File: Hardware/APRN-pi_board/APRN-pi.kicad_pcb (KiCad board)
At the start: 2 copper layers, 65 x 56.5 mm, 21 parts, among them J1 Raspberry_Pi_2_3, J2 Conn_Coaxial, J3 Amplifier Jumper, Q1 2N3906, U1 DRA818V

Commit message: Hook up voltage regulator
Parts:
- added C4: 10u, Capacitor_SMD:C_0805_2012Metric, F.Cu at (161.5, 104.5)
- added C5: 0.1u, Capacitor_SMD:C_0805_2012Metric, F.Cu at (161.0, 98.5)
- added J4: Screw_Terminal_01x02, TerminalBlock:TerminalBlock_bornier-2_P5.08mm, F.Cu at (169.5, 111.6)
- added U2: L7805, Package_TO_SOT_THT:TO-220-3_Vertical, F.Cu at (170.0, 99.5)
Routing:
- net +5V: track 81.2 -> 102.5 mm, vias 0 -> 2
- net Net-(C4-Pad1): track 0.00 -> 15.6 mm

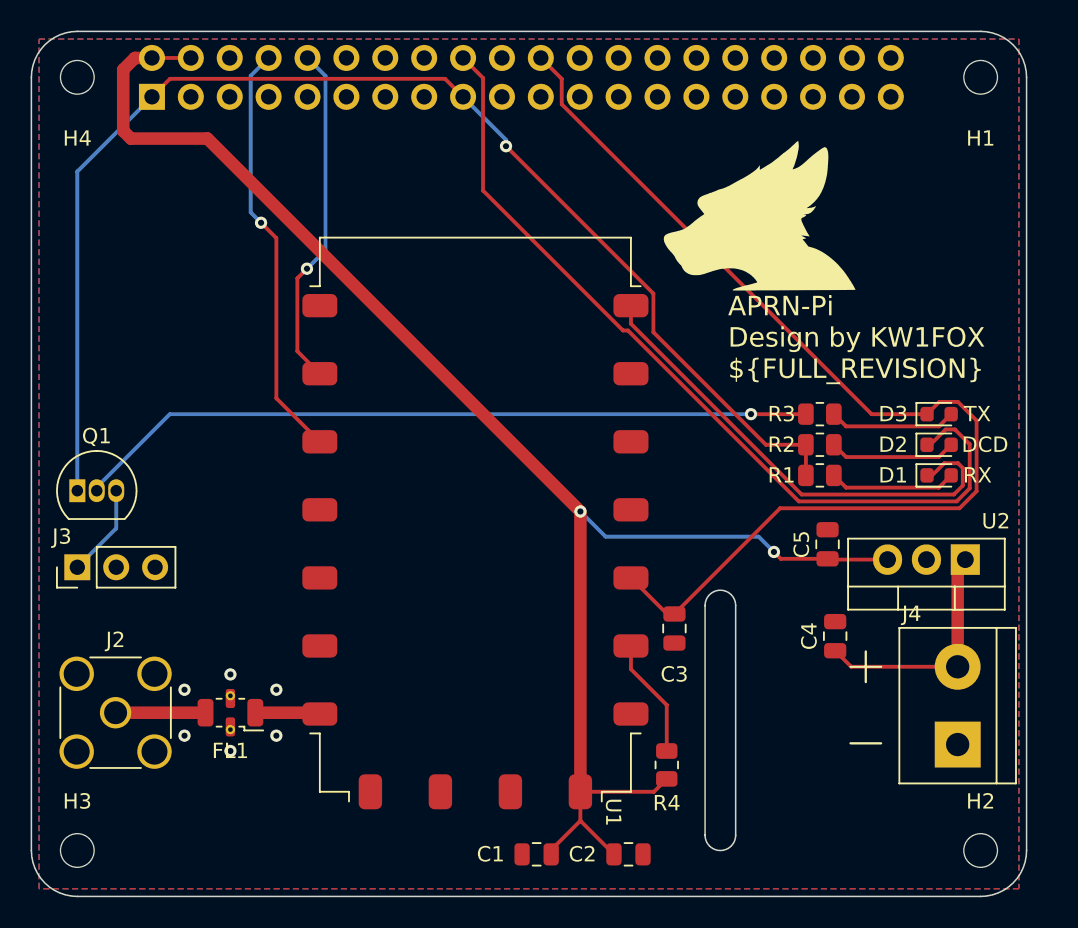
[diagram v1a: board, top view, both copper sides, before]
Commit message: More power and audio cleanup
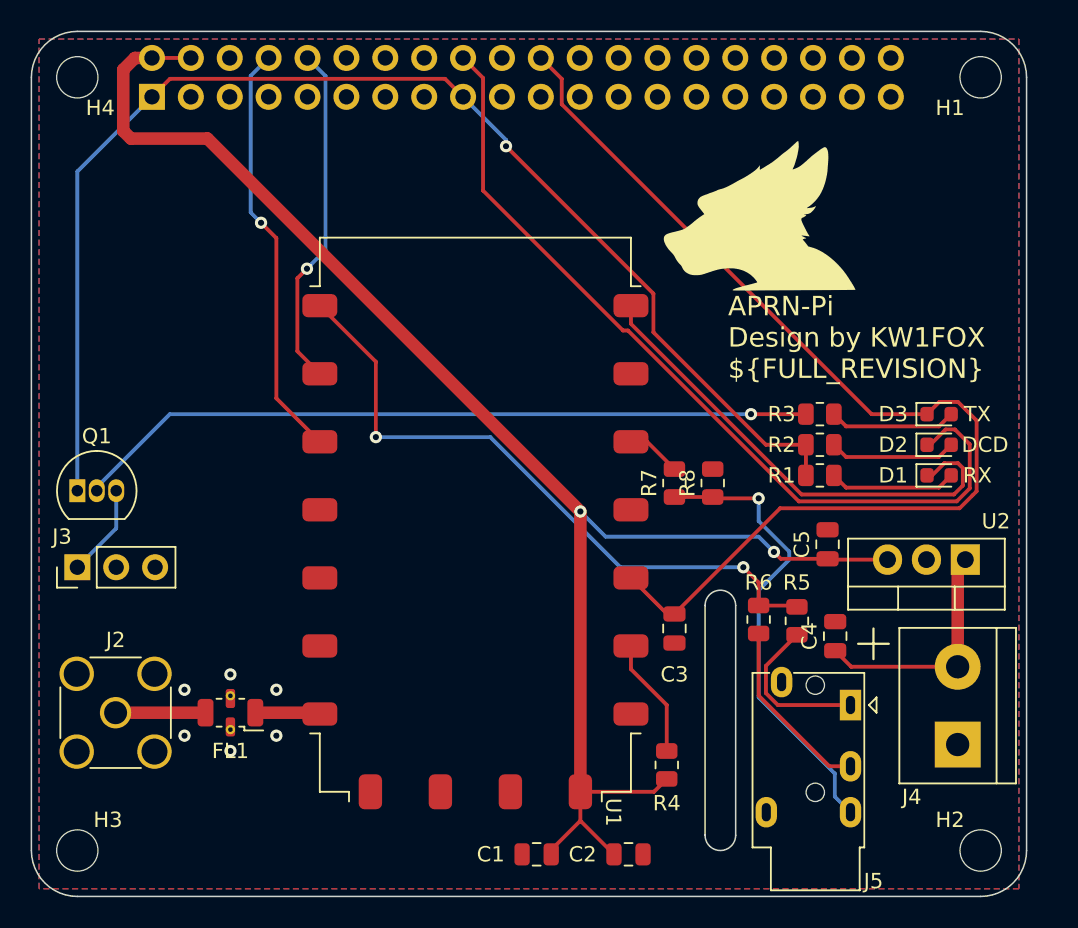
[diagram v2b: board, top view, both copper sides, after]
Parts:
- added J5: AudioJack4, Connector_Audio:Jack_3.5mm_PJ320E_Horizontal, F.Cu at (162.5, 109.0)
- added R5: 1k, Resistor_SMD:R_0805_2012Metric, F.Cu at (159.0, 103.5)
- added R6: 1k, Resistor_SMD:R_0805_2012Metric, F.Cu at (156.5, 103.4)
- added R7: 24k, Resistor_SMD:R_0805_2012Metric, F.Cu at (151.0, 94.5)
- added R8: 330, Resistor_SMD:R_0805_2012Metric, F.Cu at (153.5, 94.5)
- H1, H2, H3, H4: footprint MountingHole:MountingHole_2.2mm_M2 -> MountingHole:MountingHole_2.7mm
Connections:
- U1 pad 18: MIC -> TX_AUDIO
- U1 pad 3: unconnected-(U1-Pad3) -> RX_AUDIO
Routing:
- net TX_AUDIO: track 0.00 -> 43.1 mm, vias 0 -> 2
- net Net-(J5-PadR2): track 0.00 -> 30.2 mm, vias 0 -> 1
- net Net-(J5-PadR1): track 0.00 -> 12.0 mm
- net Net-(J5-PadT): track 0.00 -> 10.5 mm
- net RX_AUDIO: track 0.00 -> 3.58 mm

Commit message: GPIO22 should read input rx as input
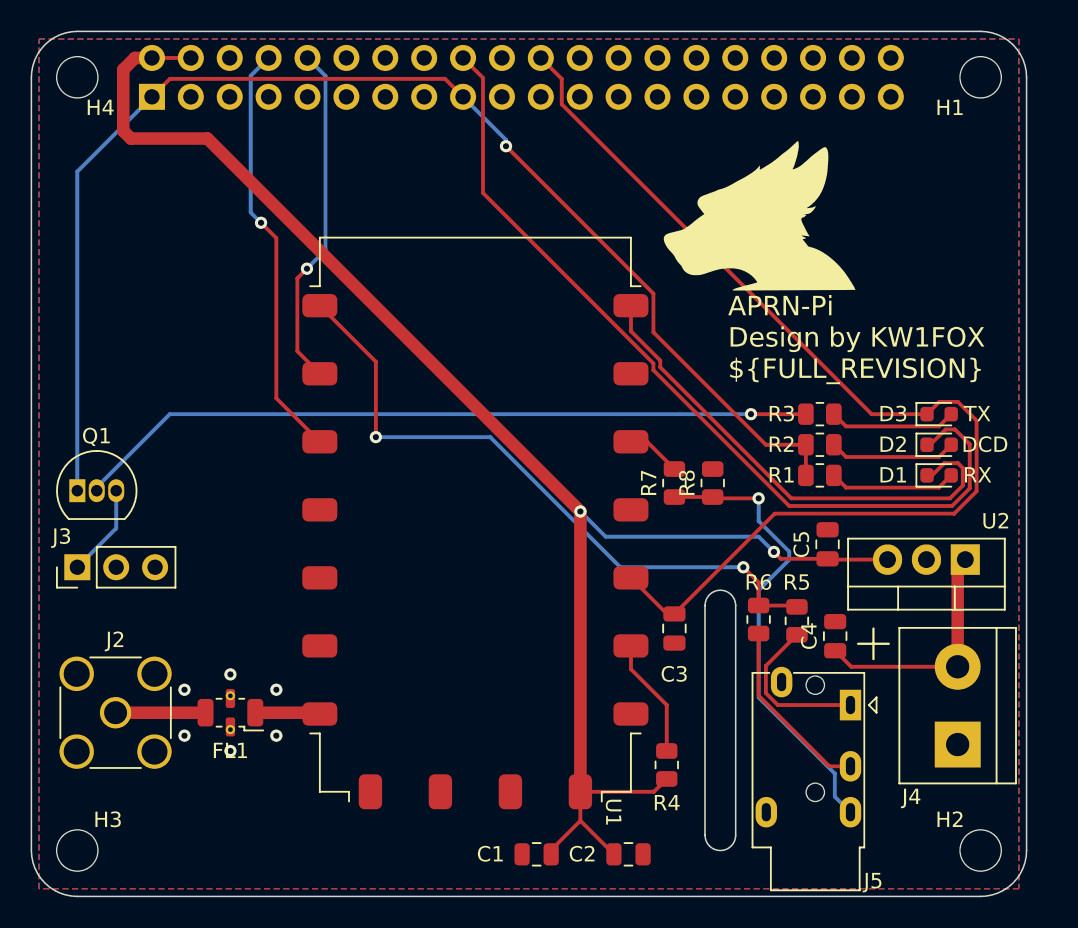
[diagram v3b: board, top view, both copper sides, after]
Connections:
- net Net-(D2-Pad1) renamed GPIO24
- D1 pad 2: Net-(D1-Pad2) -> GPIO22
- J1 pad 15: unconnected-(J1-Pad15) -> GPIO22
- R1 pad 2: Net-(D1-Pad2) -> GPIO22
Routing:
- net Net-(D1-Pad2): track 8.32 -> 0.00 mm
- net GPIO22: track 0.00 -> 8.32 mm
- net SQL: track 31.7 -> 32.4 mm
- net GPIO24: track 56.2 -> 56.8 mm

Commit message: Clean schematic a little
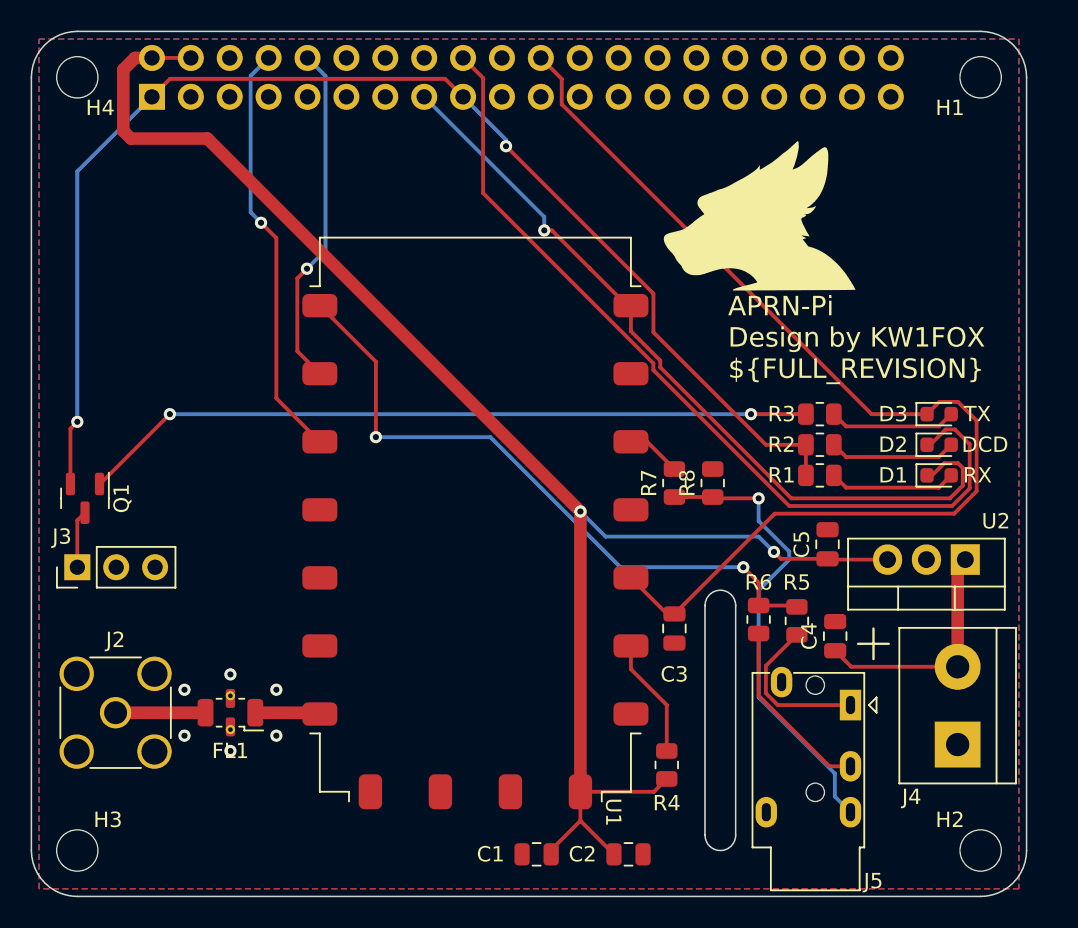
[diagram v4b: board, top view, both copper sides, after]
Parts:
- Q1: value 2N3906 -> MMBT3906; footprint Package_TO_SOT_THT:TO-92_Inline -> Package_TO_SOT_SMD:SOT-23
- moved Q1 0.71 mm to (112.5, 95.5), turned to -90 degrees
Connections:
- net PTT renamed GPIO25
- D1 pad 1: SQL -> GPIO22
- D1 pad 2: GPIO22 -> Net-(D1-Pad2)
- Q1 pad 1: +3V3 -> Net-(R3-Pad1)
- Q1 pad 2: Net-(Q1-Pad2) -> +3V3
- R1 pad 2: GPIO22 -> Net-(D1-Pad2)
- R3 pad 1: Net-(Q1-Pad2) -> Net-(R3-Pad1)
- U1 pad 1: SQL -> GPIO22
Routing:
- net Net-(Q1-Pad2): track 48.5 -> 0.00 mm, vias 1 -> 0
- net Net-(R3-Pad1): track 0.00 -> 48.0 mm, vias 0 -> 2
- net GPIO22: track 8.32 -> 52.1 mm, vias 0 -> 1
- net SQL: track 32.4 -> 0.00 mm
- net Net-(D1-Pad2): track 0.00 -> 8.32 mm
- net Net-(J3-Pad1): track 6.05 -> 3.77 mm
- net +3V3: track 84.6 -> 84.3 mm, vias 1 -> 2
